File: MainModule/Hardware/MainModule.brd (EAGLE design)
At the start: 123.2 x 100 mm, 9 parts, among them U1 ULN2803ADW, U2 ULN2803ADW, U3 ULN2803ADW, X1 MKDSN1,5/8-5,08, X2 MKDSN1,5/8-5,08, X3 MKDSN1,5/8-5,08, X4 MKDSN1,5/2-5,08, X5 MKDSN1,5/3-5,08

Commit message: 80% of the PCB design is ready.
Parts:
- added R1, R2: 10K, rcl:MINI_MELF-0204W
- added X6, X7: 057-016-0, con-panduit:057-016-0
- moved X5 26.2 mm to (37.5, -15.2)
- moved U3 4.96 mm to (67.3, 69.8)
- moved U1 2.29 mm to (47.6, 22.2)
- moved U2 2.29 mm to (67.9, 22.2)
- moved LPC1 2.01 mm to (48.9, 43.8)
- moved X3 0.64 mm to (65.4, 82.5)
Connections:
- new net N$49: LPC1.42, X6.2
- new net N$50: LPC1.47, X6.12
- new net N$51: LPC1.46, X6.10
- new net N$52: LPC1.45, X6.8
- new net N$53: LPC1.44, X6.6
- new net N$54: LPC1.53, X6.16
- new net N$55: LPC1.52, X6.14
- new net N$56: LPC1.43, X6.4
- new net N$57: LPC1.69, X7.14
- new net N$58: LPC1.70, X7.12
- new net N$59: LPC1.67, X7.10
- new net N$60: LPC1.64, X7.8
- new net N$61: LPC1.68, X7.16
- new net N$62: LPC1.61, X7.6
- new net N$63: LPC1.58, X7.4
- new net N$64: LPC1.55, X7.2
- new net SCL1: LPC1.56, X7.3
- new net SCL2: LPC1.41, R1.2, X6.3
- new net SDA1: LPC1.57, X7.5
- new net SDA2: LPC1.40, R2.2, X6.5
- new net VCC: LPC1.2, R1.1, R2.1, X6.1, X7.1
- net GND: now also X6.15, X7.15
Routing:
- net VCC: track 0.00 -> 177.2 mm
- net GND: track 0.00 -> 109.7 mm, vias 0 -> 1
- net N$53: track 0.00 -> 78.8 mm, vias 0 -> 1
- net N$56: track 0.00 -> 74.2 mm, vias 0 -> 1
- net N$55: track 0.00 -> 70.8 mm, vias 0 -> 1
- net N$52: track 0.00 -> 69.1 mm, vias 0 -> 2
- net N$54: track 0.00 -> 68.5 mm, vias 0 -> 1
- net N$51: track 0.00 -> 67.0 mm, vias 0 -> 2
- net N$50: track 0.00 -> 66.7 mm, vias 0 -> 2
- net SCL1: track 0.00 -> 64.0 mm
- net N$49: track 0.00 -> 63.7 mm
- net SDA1: track 0.00 -> 62.5 mm, vias 0 -> 1
- net SCL2: track 0.00 -> 59.4 mm, vias 0 -> 2
- net SDA2: track 0.00 -> 56.2 mm, vias 0 -> 2
- net N$40: track 0.00 -> 31.8 mm
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
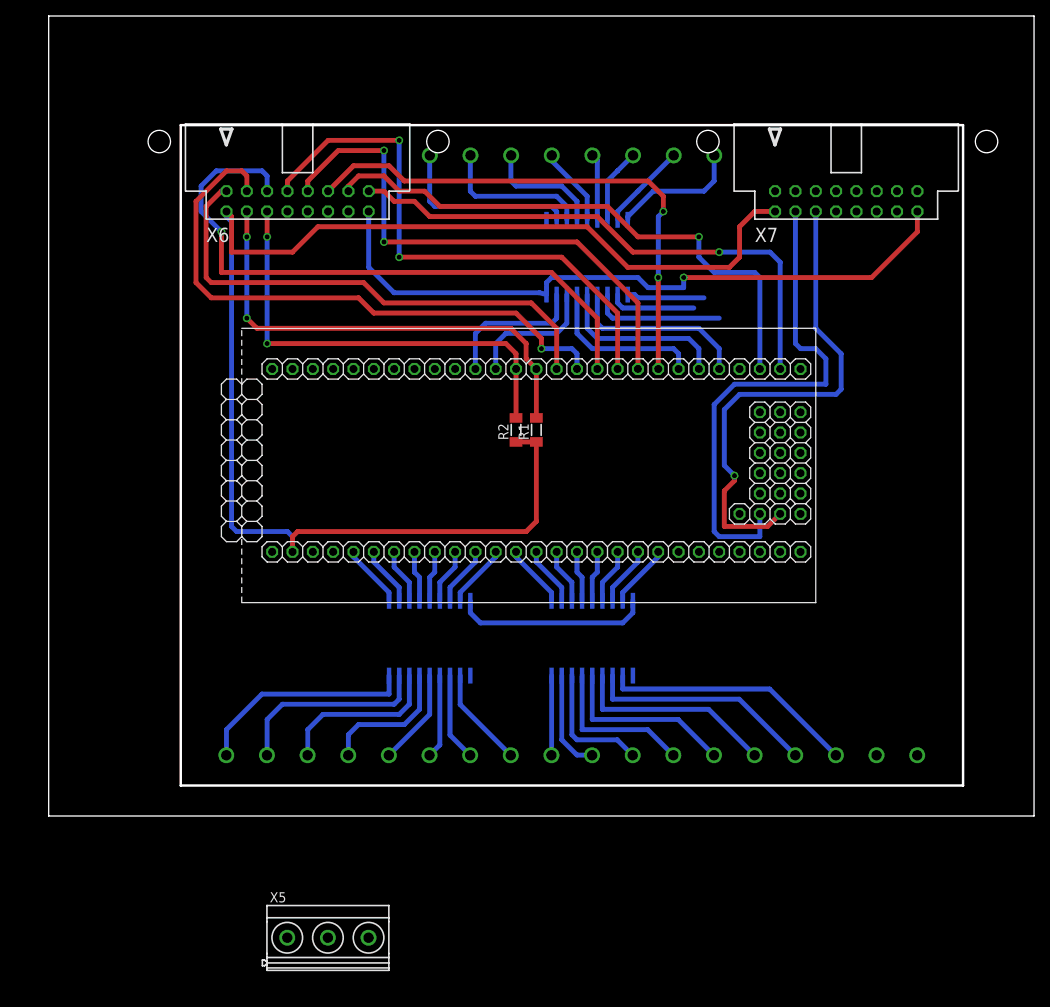
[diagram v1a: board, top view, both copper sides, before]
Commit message: 95% of PCB design is ready. (Added linear regulator)
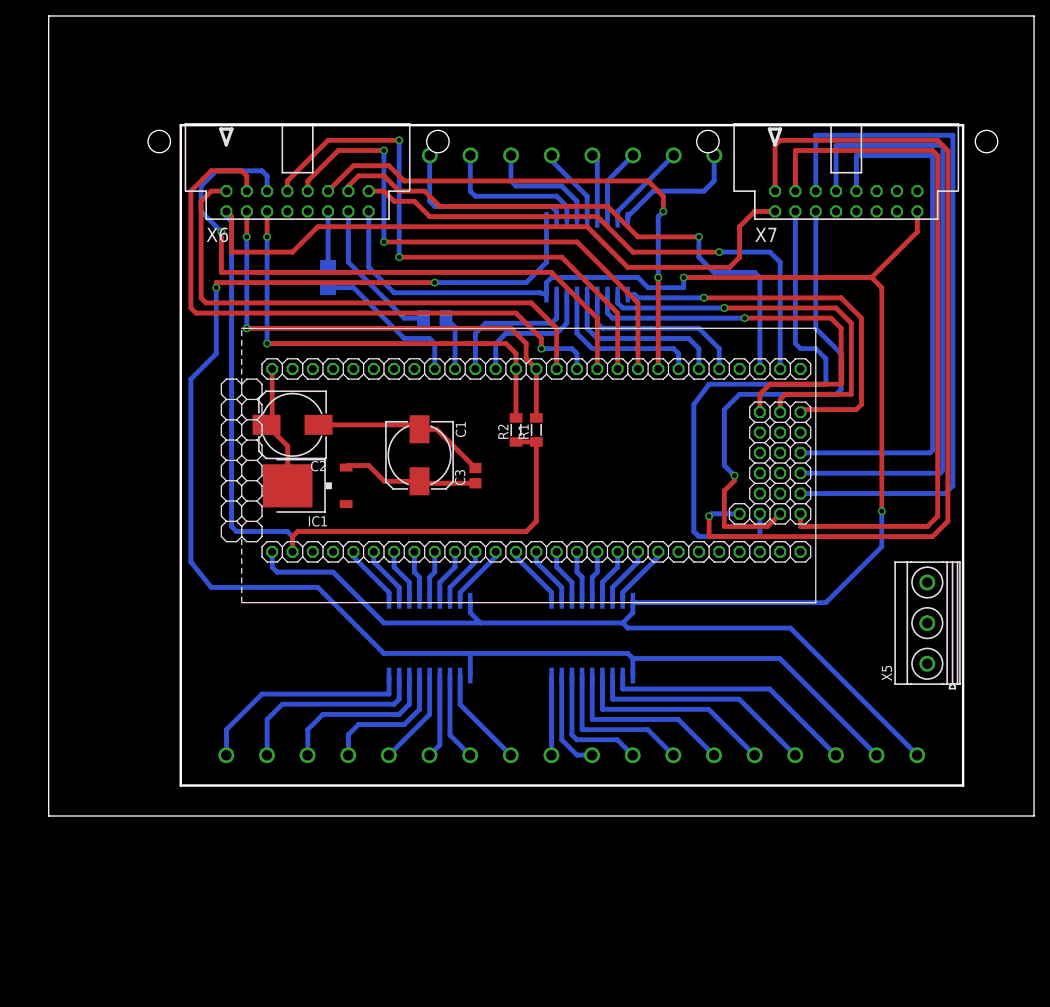
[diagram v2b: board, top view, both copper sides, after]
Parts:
- added C1: 100uF, rcl:153CLV-0810
- added C2: 10uF, rcl:153CLV-0810
- added C3: 100nF, rcl:C0805
- added IC1: MC33269D-3.3, linear:DPACK
- added R3, R4: 33, resistor:M3216
- moved X5 83.6 mm to (109.9, 26.7), turned to 90 degrees
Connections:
- removed net N$22: LPC1.73, U3.3
- removed net N$57 (its old number): LPC1.69, X7.14
- removed net N$58: LPC1.70, X7.12
- removed net N$61: LPC1.68, X7.16
- new net 3.3V: C2.+, IC1.2, LPC1.28
- new net N$65: LPC1.36, R3.1
- new net N$66: LPC1.37, R4.1
- new net N$69: LPC1.71, U3.3
- new net USB_DM: R3.2, X6.11
- new net USB_DP: R4.2, X6.13
- new net V_H: U1.10, U2.10, U3.10, X4.1
- net GND: now also C1.-, C2.-, C3.2, IC1.1, LPC1.1, X4.2
- net N$24: now also LPC1.73; no longer LPC1.71
- net VCC: now also C1.+, C3.1, IC1.3
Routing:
- net V_H: track 0.00 -> 184.7 mm, vias 0 -> 2
- net GND: track 109.7 -> 274.4 mm, vias 1 -> 2
- net N$64: track 0.00 -> 111.6 mm, vias 0 -> 1
- net N$63: track 0.00 -> 87.5 mm
- net N$62: track 0.00 -> 87.4 mm
- net N$60: track 0.00 -> 77.6 mm
- net N$57: track 0.00 -> 67.4 mm
- net N$69: track 0.00 -> 52.2 mm, vias 0 -> 1
- net N$68: track 10.8 -> 50.9 mm, vias 0 -> 1
- net N$24: track 9.69 -> 49.2 mm, vias 0 -> 1
- net N$65: track 0.00 -> 19.5 mm
- net USB_DP: track 0.00 -> 18.6 mm
- net VCC: track 177.2 -> 194.3 mm
- net N$22: track 16.5 -> 0.00 mm
- net 3.3V: track 0.00 -> 16.0 mm
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
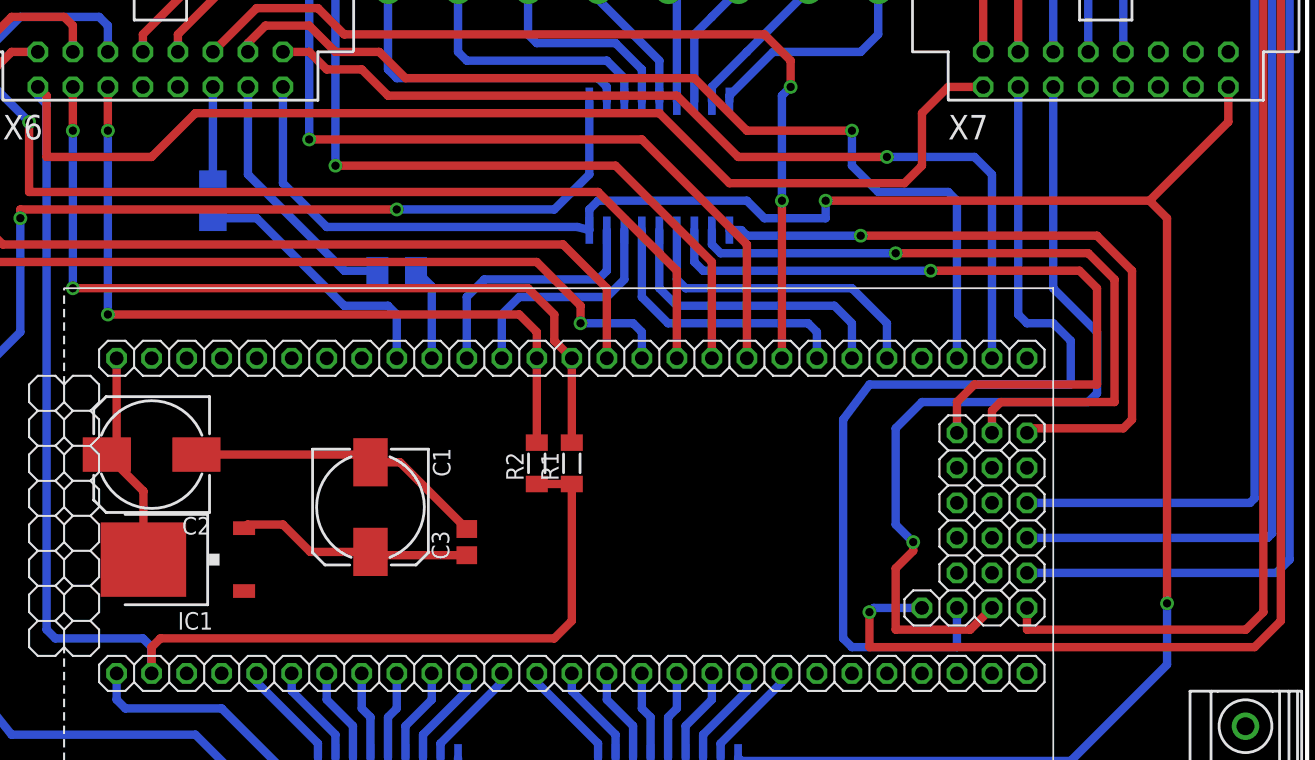
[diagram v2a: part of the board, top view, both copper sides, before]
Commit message: 99% of PCB design ready. Linear voltage regulator implementation ready.
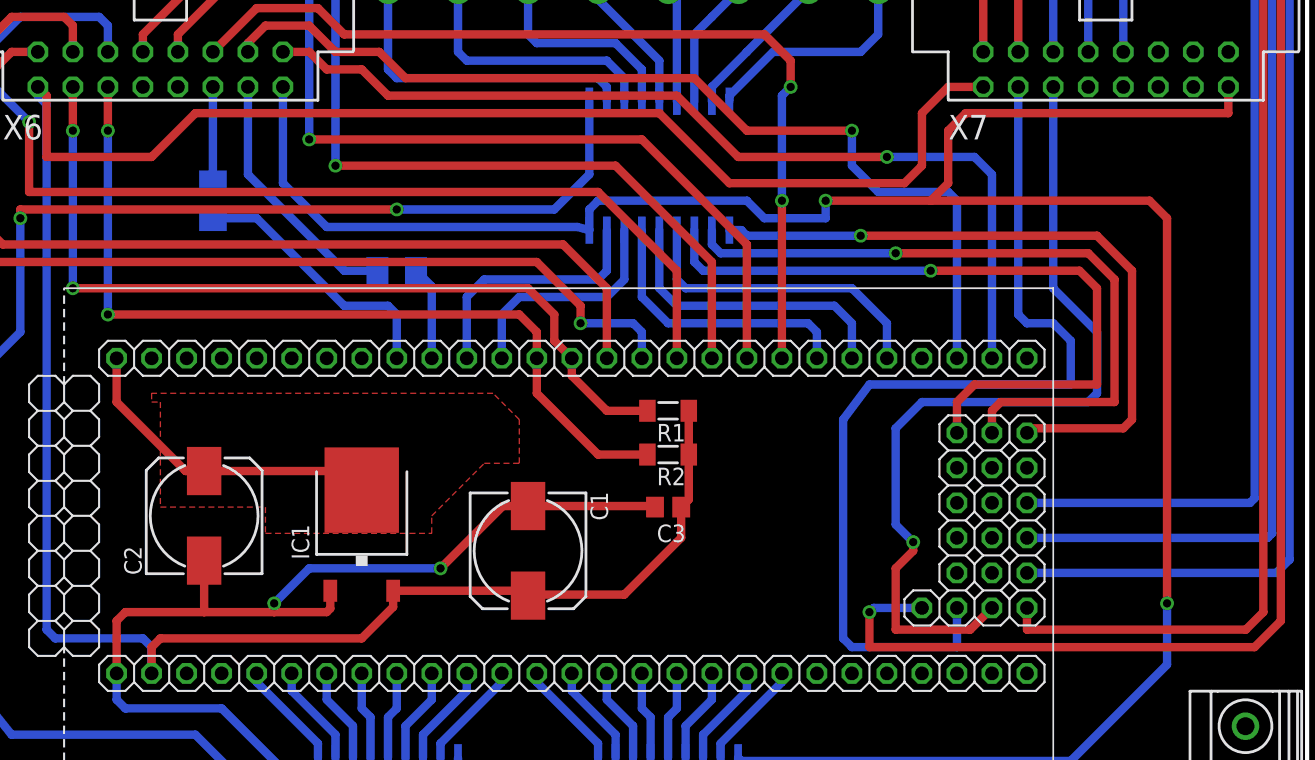
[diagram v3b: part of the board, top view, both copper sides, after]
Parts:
- moved C3 14.8 mm to (67.9, 45.1), turned to 180 degrees
- moved IC1 13.6 mm to (45.7, 43.8), turned to 0 degrees
- moved C1 11.9 mm to (57.8, 41.9)
- moved R2 9.55 mm to (67.9, 48.9), turned to 180 degrees
- moved R1 7.96 mm to (67.9, 52.1), turned to 180 degrees
- moved C2 5.85 mm to (34.3, 44.5), turned to 90 degrees
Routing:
- net GND: track 274.4 -> 326.2 mm, vias 2 -> 4
- net VCC: track 194.3 -> 185.5 mm
- net 3.3V: track 16.0 -> 23.6 mm
- net SDA2: track 56.2 -> 62.5 mm
- net SCL2: track 60.1 -> 61.8 mm
- added copper zone on layer 1, net 3.3V
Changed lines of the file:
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@@
 <attribute name="OC_FARNELL" value="unknown" x="99.695" y="80.645" size="1.778" layer="27" display="off"/>
 </element>
-<element name="R1" library="rcl" package="MINI_MELF-0204W" value="10K" x="60.96" y="48.26" rot="R90"/>
-<element name="R2" library="rcl" package="MINI_MELF-0204W" value="10K" x="58.42" y="48.26" rot="R90"/>
+<element name="R1" library="rcl" package="MINI_MELF-0204W" value="10K" x="67.945" y="52.07" rot="R180"/>
+<element name="R2" library="rcl" package="MINI_MELF-0204W" value="10K" x="67.945" y="48.895" rot="R180"/>
 <element name="R3" library="resistor" package="M3216" value="33" x="34.925" y="67.31" rot="MR90"/>
 <element name="R4" library="resistor" package="M3216" value="33" x="48.26" y="62.23" rot="MR0"/>
-<element name="IC1" library="linear" package="DPACK" value="MC33269D-3.3" x="32.385" y="41.275" rot="R90"/>
-<element name="C1" library="rcl" package="153CLV-0810" value="100uF" x="46.355" y="45.085" rot="R270"/>
-<element name="C2" library="rcl" package="153CLV-0810" value="10uF" x="30.48" y="48.895" rot="R180"/>
-<element name="C3" library="rcl" package="C0805" value="100nF" x="53.34" y="42.545" rot="R90"/>
+<element name="IC1" library="linear" package="DPACK" value="MC33269D-3.3" x="45.72" y="43.815"/>
+<element name="C1" library="rcl" package="153CLV-0810" value="100uF" x="57.785" y="41.91" rot="R270"/>
+<element name="C2" library="rcl" package="153CLV-0810" value="10uF" x="34.29" y="44.45" rot="R90"/>
+<element name="C3" library="rcl" package="C0805" value="100nF" x="67.945" y="45.085" rot="R180"/>
 </elements>
 <signals>
@@
 <wire x1="43.18" y1="65.405" x2="61.3664" y2="65.405" width="0.6096" layer="16"/>
 <wire x1="61.3664" y1="65.405" x2="62.23" y2="65.1764" width="0.6096" layer="16"/>
-<wire x1="108.585" y1="75.565" x2="108.585" y2="73.025" width="0.6096" layer="1"/>
-<wire x1="108.585" y1="73.025" x2="102.87" y2="67.31" width="0.6096" layer="1"/>
+<wire x1="108.585" y1="75.565" x2="108.585" y2="73.66" width="0.6096" layer="1"/>
 <via x="79.375" y="67.31" extent="1-16" drill="0.6" shape="square"/>
 <wire x1="62.23" y1="65.1764" x2="62.23" y2="66.675" width="0.6096" layer="16"/>
@@
 <wire x1="74.93" y1="66.04" x2="79.375" y2="66.04" width="0.6096" layer="16"/>
 <wire x1="79.375" y1="66.04" x2="79.375" y2="67.31" width="0.6096" layer="16"/>
-<wire x1="79.375" y1="67.31" x2="102.87" y2="67.31" width="0.6096" layer="1"/>
+<wire x1="79.375" y1="67.31" x2="86.995" y2="67.31" width="0.6096" layer="1"/>
+<wire x1="86.995" y1="67.31" x2="102.87" y2="67.31" width="0.6096" layer="1"/>
 <wire x1="102.87" y1="67.31" x2="104.14" y2="66.04" width="0.6096" layer="1"/>
 <wire x1="104.14" y1="66.04" x2="104.14" y2="38.1" width="0.6096" layer="1"/>
@@
 <contactref element="IC1" pad="1"/>
 <contactref element="C3" pad="2"/>
-<wire x1="33.73" y1="48.895" x2="45.795" y2="48.895" width="0.6096" layer="1"/>
-<wire x1="45.795" y1="48.895" x2="46.355" y2="48.335" width="0.6096" layer="1"/>
-<wire x1="35.56" y1="30.48" x2="37.185" y2="38.995" width="0" layer="19" extent="1-16"/>
-<wire x1="46.355" y1="48.335" x2="48.5" y2="48.335" width="0.6096" layer="1"/>
-<wire x1="48.5" y1="48.335" x2="53.34" y2="43.495" width="0.6096" layer="1"/>
-<wire x1="37.185" y1="38.995" x2="33.73" y2="48.895" width="0" layer="19" extent="1-1"/>
+<wire x1="57.785" y1="45.16" x2="66.92" y2="45.16" width="0.6096" layer="1"/>
+<wire x1="66.92" y1="45.16" x2="66.995" y2="45.085" width="0.6096" layer="1"/>
+<wire x1="43.44" y1="39.015" x2="43.44" y2="37.725" width="0.6096" layer="1"/>
+<wire x1="43.44" y1="37.725" x2="43.18" y2="37.465" width="0.6096" layer="1"/>
+<wire x1="43.18" y1="37.465" x2="39.37" y2="37.465" width="0.6096" layer="1"/>
+<wire x1="39.37" y1="37.465" x2="34.29" y2="37.465" width="0.6096" layer="1"/>
+<wire x1="34.29" y1="37.465" x2="28.575" y2="37.465" width="0.6096" layer="1"/>
+<wire x1="28.575" y1="37.465" x2="27.94" y2="36.83" width="0.6096" layer="1"/>
+<wire x1="27.94" y1="36.83" x2="27.94" y2="33.02" width="0.6096" layer="1"/>
+<wire x1="34.29" y1="41.2" x2="34.29" y2="37.465" width="0.6096" layer="1"/>
+<wire x1="57.785" y1="45.16" x2="55.955" y2="45.16" width="0.6096" layer="1"/>
+<wire x1="55.955" y1="45.16" x2="51.435" y2="40.64" width="0.6096" layer="1"/>
+<via x="51.435" y="40.64" extent="1-16" drill="0.6" shape="square"/>
+<wire x1="51.435" y1="40.64" x2="41.91" y2="40.64" width="0.6096" layer="16"/>
+<wire x1="41.91" y1="40.64" x2="39.37" y2="38.1" width="0.6096" layer="16"/>
+<via x="39.37" y="38.1" extent="1-16" drill="0.6" shape="square"/>
+<wire x1="39.37" y1="38.1" x2="39.37" y2="37.465" width="0.6096" layer="1"/>
+<wire x1="108.585" y1="73.66" x2="89.535" y2="73.66" width="0.6096" layer="1"/>
+<wire x1="89.535" y1="73.66" x2="88.265" y2="72.39" width="0.6096" layer="1"/>
+<wire x1="88.265" y1="72.39" x2="88.265" y2="68.58" width="0.6096" layer="1"/>
+<wire x1="88.265" y1="68.58" x2="86.995" y2="67.31" width="0.6096" layer="1"/>
 </signal>
 <signal name="N$9">
@@
 <contactref element="R2" pad="1"/>
 <contactref element="R1" pad="1"/>
-<wire x1="60.96" y1="36.83" x2="59.69" y2="35.56" width="0.6096" layer="1"/>
-<wire x1="60.96" y1="46.76" x2="58.42" y2="46.76" width="0.6096" layer="1"/>
-<wire x1="60.96" y1="36.83" x2="60.96" y2="46.76" width="0.6096" layer="1"/>
-<wire x1="59.69" y1="35.56" x2="31.115" y2="35.56" width="0.6096" layer="1"/>
 <wire x1="22.225" y1="75.565" x2="22.225" y2="74.93" width="0.6096" layer="16"/>
 <wire x1="22.225" y1="74.93" x2="22.86" y2="74.295" width="0.6096" layer="16"/>
@@
 <contactref element="C3" pad="1"/>
 <contactref element="C1" pad="+"/>
-<wire x1="53.34" y1="41.595" x2="46.595" y2="41.595" width="0.6096" layer="1"/>
-<wire x1="46.595" y1="41.595" x2="46.355" y2="41.835" width="0.6096" layer="1"/>
-<wire x1="46.355" y1="41.835" x2="41.985" y2="41.835" width="0.6096" layer="1"/>
-<wire x1="41.985" y1="41.835" x2="40.005" y2="43.815" width="0.6096" layer="1"/>
-<wire x1="40.005" y1="43.815" x2="37.445" y2="43.815" width="0.6096" layer="1"/>
-<wire x1="37.445" y1="43.815" x2="37.185" y2="43.555" width="0.6096" layer="1"/>
-<wire x1="58.42" y1="46.76" x2="53.34" y2="41.595" width="0" layer="19" extent="1-1"/>
+<wire x1="69.445" y1="52.07" x2="69.445" y2="48.895" width="0.6096" layer="1"/>
+<wire x1="69.445" y1="48.895" x2="69.445" y2="45.635" width="0.6096" layer="1"/>
+<wire x1="69.445" y1="45.635" x2="68.895" y2="45.085" width="0.6096" layer="1"/>
+<wire x1="48" y1="39.015" x2="57.43" y2="39.015" width="0.6096" layer="1"/>
+<wire x1="57.43" y1="39.015" x2="57.785" y2="38.66" width="0.6096" layer="1"/>
+<wire x1="68.895" y1="45.085" x2="68.895" y2="42.86" width="0.6096" layer="1"/>
+<wire x1="68.895" y1="42.86" x2="64.77" y2="38.735" width="0.6096" layer="1"/>
+<wire x1="64.77" y1="38.735" x2="57.86" y2="38.735" width="0.6096" layer="1"/>
+<wire x1="57.86" y1="38.735" x2="57.785" y2="38.66" width="0.6096" layer="1"/>
+<wire x1="48" y1="39.015" x2="48" y2="37.84" width="0.6096" layer="1"/>
+<wire x1="48" y1="37.84" x2="45.72" y2="35.56" width="0.6096" layer="1"/>
+<wire x1="45.72" y1="35.56" x2="31.115" y2="35.56" width="0.6096" layer="1"/>
 </signal>
 <signal name="SCL1">
@@
 <wire x1="27.305" y1="72.39" x2="27.305" y2="75.565" width="0.6096" layer="1"/>
 <contactref element="R2" pad="2"/>
-<wire x1="58.42" y1="49.76" x2="58.42" y2="55.88" width="0.6096" layer="1"/>
+<wire x1="66.445" y1="48.895" x2="62.865" y2="48.895" width="0.6096" layer="1"/>
+<wire x1="62.865" y1="48.895" x2="58.42" y2="53.34" width="0.6096" layer="1"/>
+<wire x1="58.42" y1="53.34" x2="58.42" y2="55.88" width="0.6096" layer="1"/>
 </signal>
 <signal name="SCL2">
@@
 <wire x1="24.765" y1="72.39" x2="24.765" y2="75.565" width="0.6096" layer="1"/>
 <contactref element="R1" pad="2"/>
-<wire x1="60.96" y1="49.76" x2="60.96" y2="55.88" width="0.6096" layer="1"/>
+<wire x1="66.445" y1="52.07" x2="63.5" y2="52.07" width="0.6096" layer="1"/>
+<wire x1="63.5" y1="52.07" x2="60.96" y2="54.61" width="0.6096" layer="1"/>
+<wire x1="60.96" y1="54.61" x2="60.96" y2="55.88" width="0.6096" layer="1"/>
 </signal>
 <signal name="N$60">
@@
 <contactref element="C2" pad="+"/>
 <contactref element="LPC1" pad="28"/>
-<wire x1="29.885" y1="41.275" x2="29.885" y2="46.24" width="0.6096" layer="1"/>
-<wire x1="29.885" y1="46.24" x2="27.23" y2="48.895" width="0.6096" layer="1"/>
-<wire x1="27.94" y1="55.88" x2="27.94" y2="49.605" width="0.6096" layer="1"/>
-<wire x1="27.94" y1="49.605" x2="27.23" y2="48.895" width="0.6096" layer="1"/>
+<wire x1="34.29" y1="47.7" x2="32.945" y2="47.7" width="0.6096" layer="1"/>
+<wire x1="32.945" y1="47.7" x2="27.94" y2="52.705" width="0.6096" layer="1"/>
+<wire x1="27.94" y1="52.705" x2="27.94" y2="55.88" width="0.6096" layer="1"/>
+<wire x1="34.29" y1="47.7" x2="44.335" y2="47.7" width="0.6096" layer="1"/>
+<wire x1="44.335" y1="47.7" x2="45.72" y2="46.315" width="0.6096" layer="1"/>
+<polygon width="0.254" layer="1">
+<vertex x="30.48" y="52.705"/>
+<vertex x="31.115" y="52.705"/>
+<vertex x="31.115" y="45.085"/>
+<vertex x="38.735" y="45.085"/>
+<vertex x="38.735" y="43.18"/>
+<vertex x="50.8" y="43.18"/>
+<vertex x="50.8" y="44.45"/>
+<vertex x="54.61" y="48.26"/>
+<vertex x="57.15" y="48.26"/>
+<vertex x="57.15" y="51.435"/>
+<vertex x="55.245" y="53.34"/>
+<vertex x="30.48" y="53.34"/>
+</polygon>
 </signal>
 </signals>
